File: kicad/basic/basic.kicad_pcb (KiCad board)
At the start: 2 copper layers, 50 x 50 mm, 20 parts, among them P2 CONN_01X15, P3 CONN_01X15, P4 CONN_01X06, P5 CONN_01X01, P6 CONN_01X01, P7 CONN_01X01, P8 CONN_01X01, P9 CONN_01X06, SW1 SW_PUSH, SW2 SW_PUSH

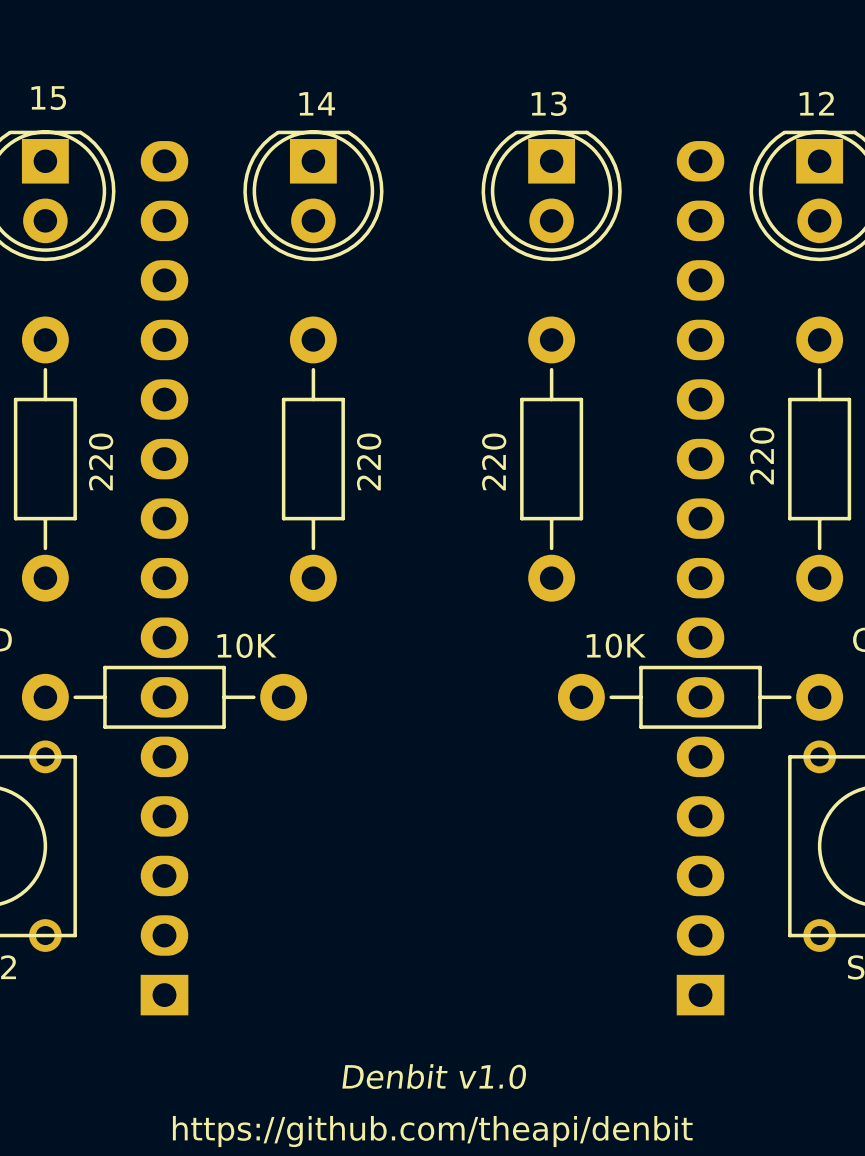
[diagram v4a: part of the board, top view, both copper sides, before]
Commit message: Swapped headers
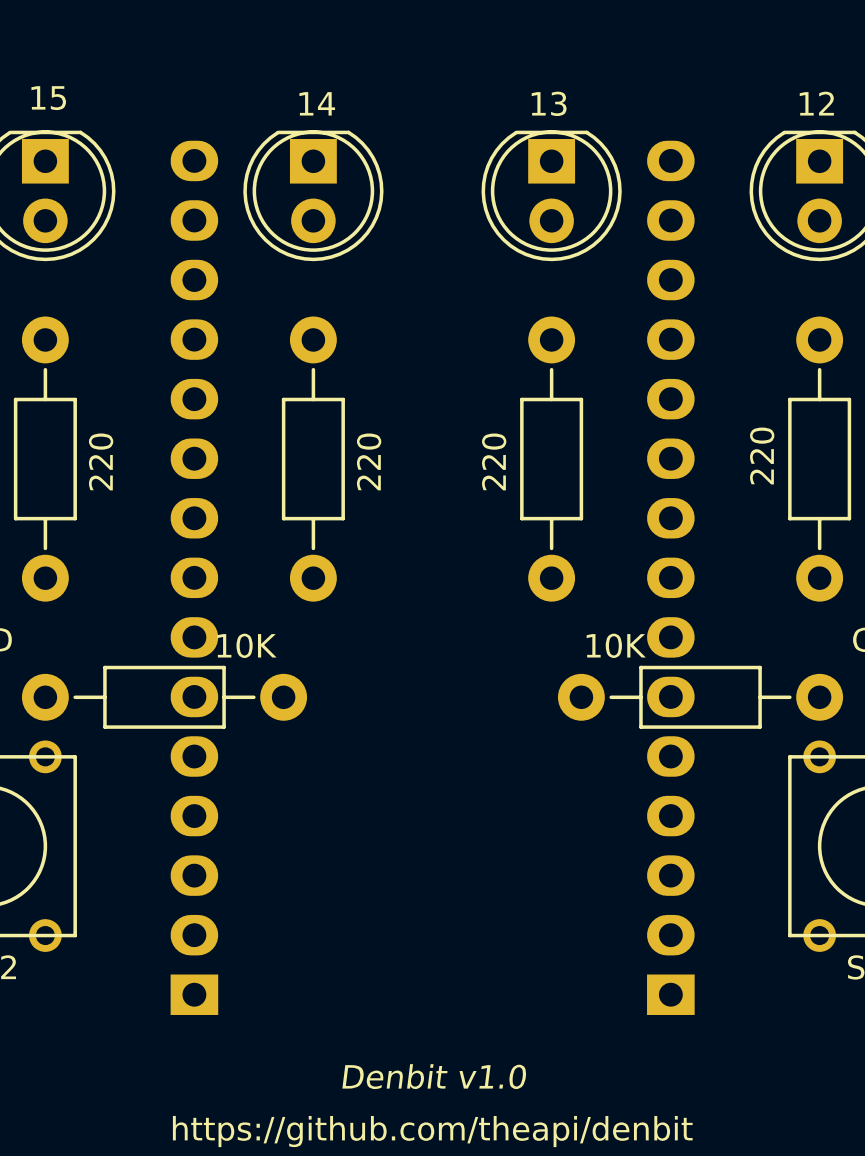
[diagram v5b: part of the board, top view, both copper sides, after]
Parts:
- moved P2 21.6 mm to (155.5, 114.6)
- moved P3 21.6 mm to (135.2, 114.6)
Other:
- board text added: "USB"
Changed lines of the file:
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@@
     (area 115.226999 66.712999 175.427001 135.073001)
     (thickness 1.6)
-    (drawings 29)
+    (drawings 35)
     (tracks 0)
     (zones 0)
@@
     (aux_axis_origin 0 0)
     (grid_origin 145.332 96.81)
-    (visible_elements FFFFFF7F)
+    (visible_elements FFFFF77F)
     (pcbplotparams
       (layerselection 0x00030_80000001)
@@
   )
   (module Socket_Strips:Socket_Strip_Straight_1x15 (layer B.Cu)
-    (at 133.897 114.605 90)
+    (at 155.492 114.59 90)
     (descr "Through hole socket strip")
     (tags "socket strip")
@@
   )
   (module Socket_Strips:Socket_Strip_Straight_1x15 (layer B.Cu)
-    (at 156.757 114.605 90)
+    (at 135.172 114.59 90)
     (descr "Through hole socket strip")
     (tags "socket strip")
@@
     )
   )
+  (gr_text USB (at 145.332 119.416) (layer B.SilkS)
+    (effects (font (size 1 1) (thickness 0.15)) (justify mirror))
+  )
+  (gr_line (start 150.158 117.892) (end 150.158 121.956) (angle 90) (layer B.SilkS) (width 0.2))
+  (gr_line (start 149.142 116.876) (end 150.158 117.892) (angle 90) (layer B.SilkS) (width 0.2))
+  (gr_line (start 141.522 116.876) (end 149.142 116.876) (angle 90) (layer B.SilkS) (width 0.2))
+  (gr_line (start 140.506 117.892) (end 141.522 116.876) (angle 90) (layer B.SilkS) (width 0.2))
+  (gr_line (start 140.506 121.702) (end 140.506 117.892) (angle 90) (layer B.SilkS) (width 0.2))
   (gr_text https://github.com/theapi/denbit (at 145.292 120.34) (layer F.SilkS)
     (effects (font (size 1 1) (thickness 0.15)))

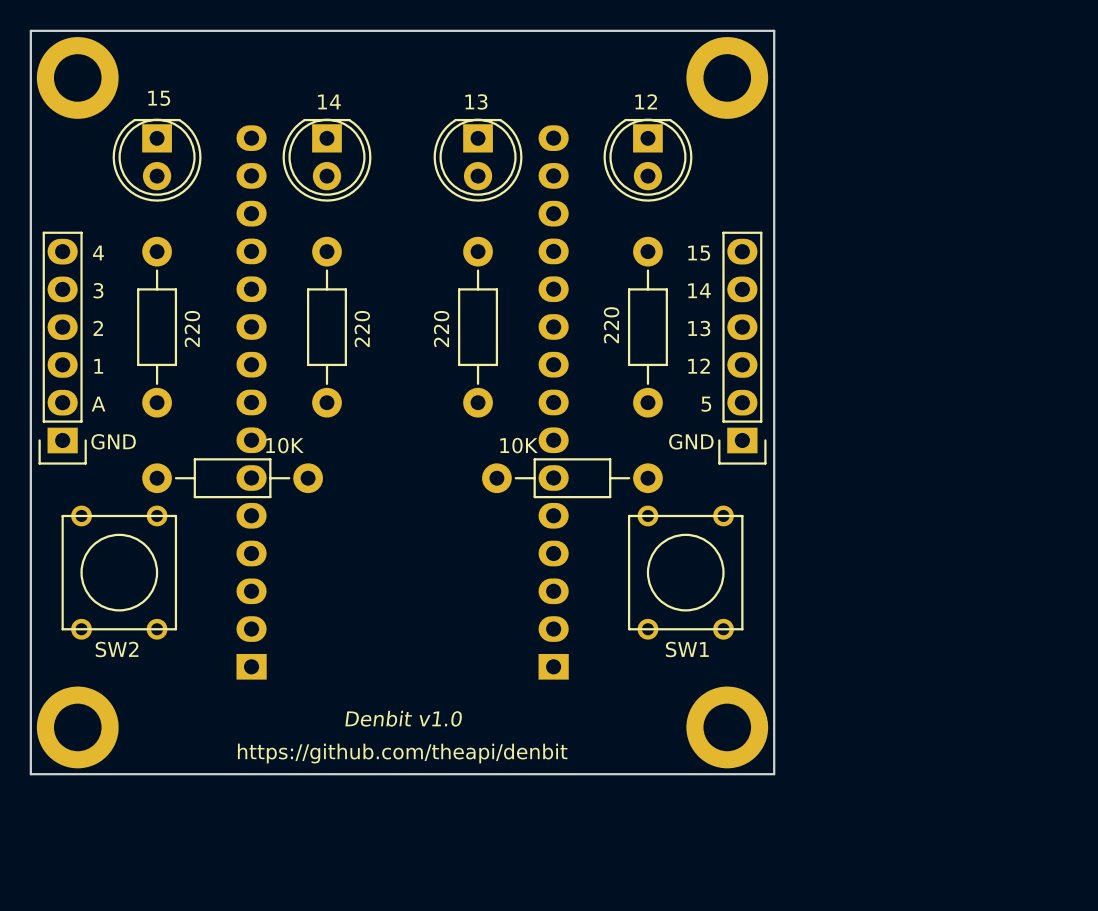
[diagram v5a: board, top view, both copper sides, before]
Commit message: Corrected footprint width
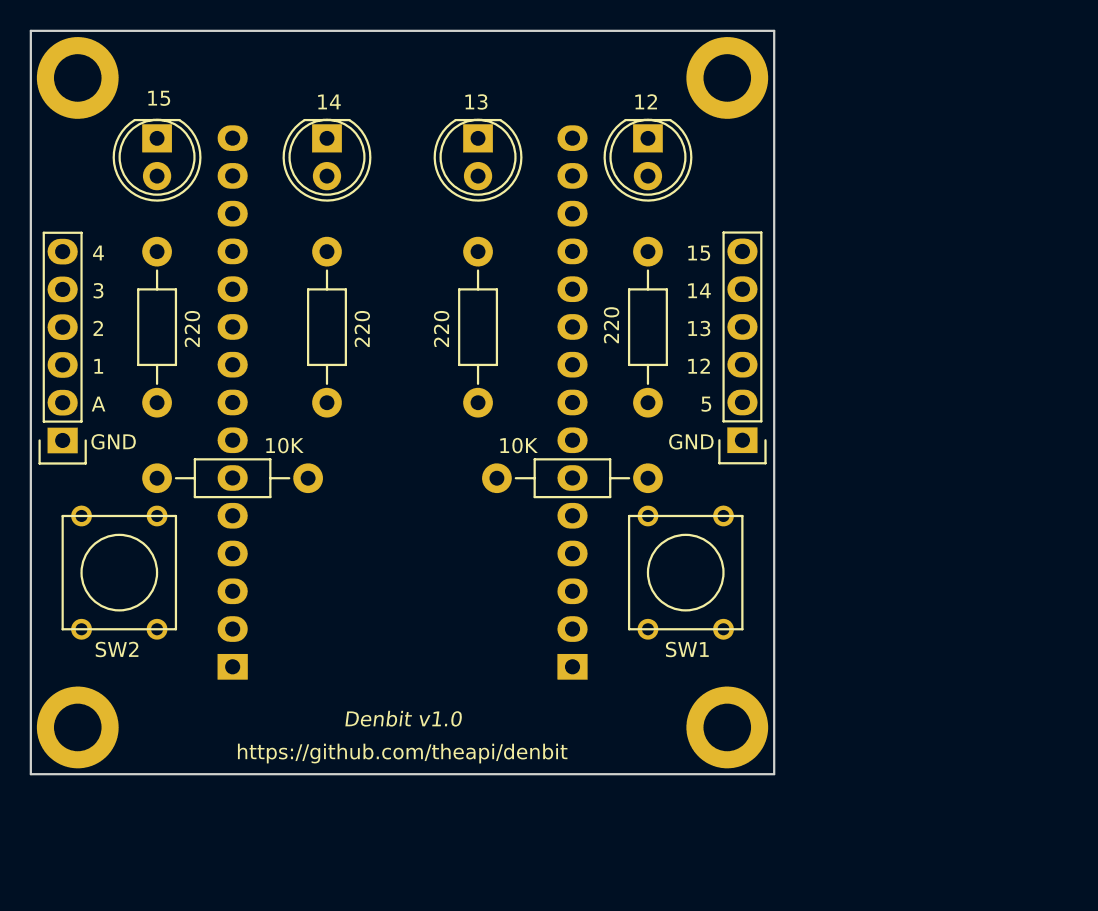
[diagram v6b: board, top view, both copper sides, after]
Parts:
- moved P2 1.27 mm to (156.8, 114.6)
- moved P3 1.27 mm to (133.9, 114.6)
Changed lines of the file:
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@@
-(kicad_pcb (version 4) (host pcbnew 4.0.2-4+6225~38~ubuntu14.04.1-stable)
+(kicad_pcb (version 4) (host pcbnew 4.0.1-stable)
   (general
     (links 44)
@@
     (aux_axis_origin 0 0)
     (grid_origin 145.332 96.81)
-    (visible_elements FFFFF77F)
+    (visible_elements 7FFFF7FF)
     (pcbplotparams
       (layerselection 0x00030_80000001)
@@
   )
   (module Socket_Strips:Socket_Strip_Straight_1x15 (layer B.Cu)
-    (at 155.492 114.59 90)
+    (at 156.762 114.59 90)
     (descr "Through hole socket strip")
     (tags "socket strip")
@@
   )
   (module Socket_Strips:Socket_Strip_Straight_1x15 (layer B.Cu)
-    (at 135.172 114.59 90)
+    (at 133.902 114.59 90)
     (descr "Through hole socket strip")
     (tags "socket strip")
@@
   )
   (module Socket_Strips:Socket_Strip_Straight_1x06 (layer F.Cu)
-    (at 168.187 99.365 90)
+    (at 168.192 99.35 90)
     (descr "Through hole socket strip")
     (tags "socket strip")

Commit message: Routing
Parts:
- moved P4 45.7 mm to (168.2, 99.3)
- moved P9 45.7 mm to (122.5, 99.3)
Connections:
- P2 pad 1: A0 -> Net-(P2-Pad1)
- P2 pad 10: GND -> Net-(P2-Pad10)
- P2 pad 11: 3V3 -> Net-(P2-Pad11)
- P2 pad 14: GND -> Net-(P2-Pad14)
- P2 pad 15: Net-(P2-Pad15) -> A0
- P2 pad 2: Net-(P2-Pad2) -> GND
- P2 pad 5: Net-(P2-Pad5) -> 3V3
- P2 pad 6: Net-(P2-Pad6) -> GND
- P3 pad 10: 3V3 -> Net-(P3-Pad10)
- P3 pad 11: GIPO2 -> D4
- P3 pad 12: GIPO0 -> D3
- P3 pad 13: GIPO4 -> D2
- P3 pad 14: GIPO5 -> D1
- P3 pad 3: GPIO1 -> D10
- P3 pad 4: GIPO3 -> D9
- P3 pad 5: GIPO15 -> D8
- P3 pad 6: GIPO13 -> D7
- P3 pad 7: GIPO12 -> D6
- P3 pad 8: GIPO14 -> Net-(P3-Pad8)
- P4 pad 2: A0 -> D4
- P4 pad 3: GIPO1 -> D3
- P4 pad 4: GIPO2 -> D2
- P4 pad 5: GIPO3 -> D1
- P4 pad 6: GIPO4 -> A0
- P9 pad 2: GIPO5 -> D10
- P9 pad 3: GIPO12 -> D9
- P9 pad 4: GIPO13 -> D8
- P9 pad 5: GIPO14 -> D7
- P9 pad 6: GIPO15 -> D6
- R1 pad 2: GIPO5 -> D1
- R2 pad 2: GIPO4 -> D2
- R3 pad 2: GIPO15 -> D7
- R4 pad 2: GIPO12 -> D10
- R5 pad 2: GIPO14 -> D8
- R6 pad 2: GIPO13 -> D9
- SW1 pad 2: GIPO5 -> D1
- SW2 pad 2: GIPO4 -> D2
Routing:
- net GND: track 0.00 -> 177.0 mm
- net D1: track 0.00 -> 70.8 mm
- net D2: track 0.00 -> 69.2 mm
- net 3V3: track 0.00 -> 68.0 mm
- net D10: track 0.00 -> 53.1 mm
- net D9: track 0.00 -> 42.0 mm
- net D4: track 0.00 -> 38.5 mm
- net D3: track 0.00 -> 37.4 mm
- net D8: track 0.00 -> 30.8 mm
- net A0: track 0.00 -> 21.0 mm
- net D6: track 0.00 -> 19.5 mm
- net D7: track 0.00 -> 19.3 mm
- net Net-(D4-Pad2): track 0.00 -> 5.08 mm
- net Net-(D3-Pad2): track 0.00 -> 5.07 mm
- net Net-(D2-Pad2): track 0.00 -> 5.07 mm
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- added copper zone on B.Cu, net GND
- added copper zone on F.Cu, net GND
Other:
- board text added: "A0"
- board text added: "D1"
- board text added: "D10"
- board text added: "D2"
- board text added: "D3"
- board text added: "D4"
- board text added: "D6"
- board text added: "D7"
- board text added: "D8"
- board text added: "D9"
- board text removed: "1"
- board text removed: "12"
- board text removed: "13"
- board text removed: "14"
- board text removed: "15"
- board text removed: "2"
- board text removed: "3"
- board text removed: "4"
- board text removed: "5"
- board text removed: "A"

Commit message: Dennis logo
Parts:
- added G***: LOGO, denbit:LOGO, F.Cu at (145.8, 113.6)
